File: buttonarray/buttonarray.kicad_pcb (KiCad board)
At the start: 2 copper layers, 129.5 x 106.7 mm, 103 parts, among them J1 CtrlPins, Q1 2N2219, Q10 2N2219, Q11 2N2219, Q12 2N2219, Q13 2N2219, Q14 2N2219, Q15 2N2219, Q16 2N2219, Q2 2N2219, Q3 2N2219, Q4 2N2219, Q5 2N2219, Q6 2N2219, Q7 2N2219, Q8 2N2219, Q9 2N2219, SW1 SW_Push_LED, SW10 SW_Push_LED, SW11 SW_Push_LED, SW12 SW_Push_LED, SW13 SW_Push_LED, SW14 SW_Push_LED, SW15 SW_Push_LED, SW16 SW_Push_LED, SW17 Addr_DIP_SW, SW2 SW_Push_LED, SW3 SW_Push_LED, SW4 SW_Push_LED, SW5 SW_Push_LED, SW6 SW_Push_LED, SW7 SW_Push_LED, SW8 SW_Push_LED, SW9 SW_Push_LED, U1 LM2575-3.3BT

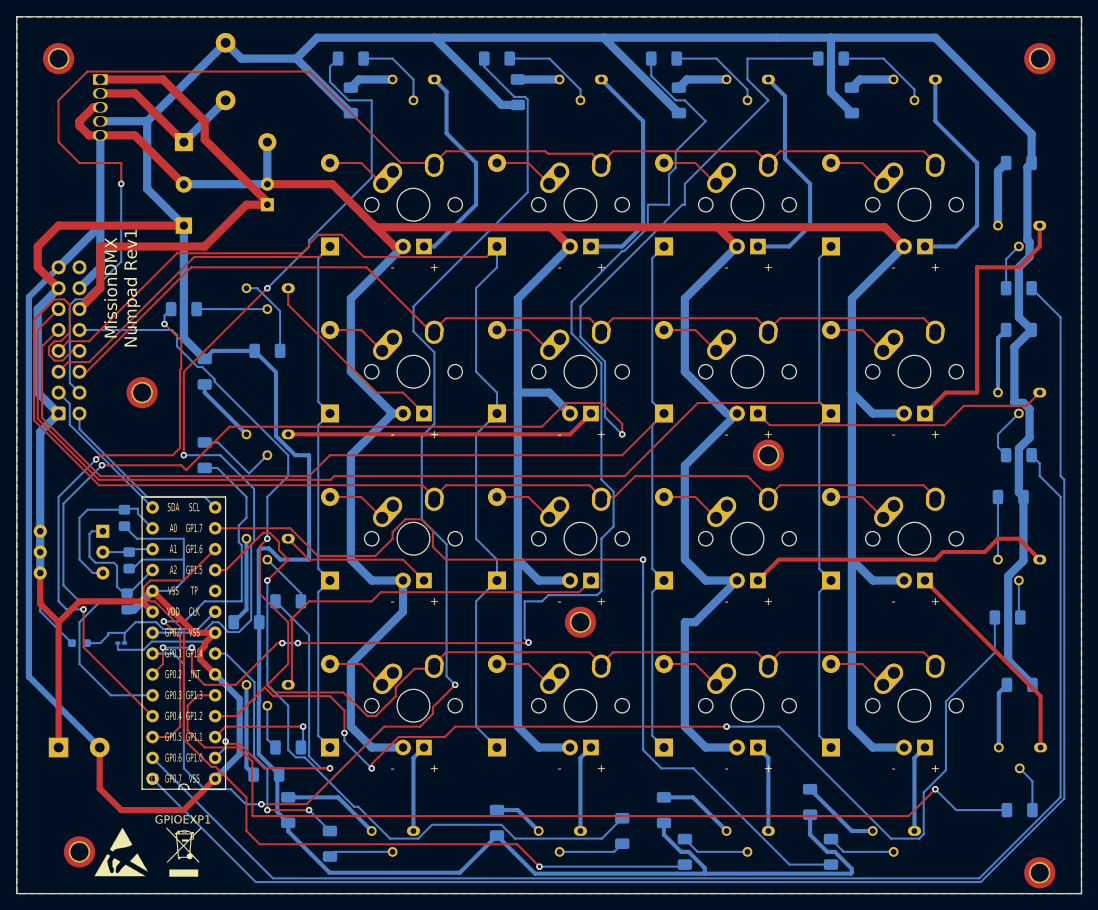
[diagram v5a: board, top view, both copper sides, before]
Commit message: chg: button array rev 1
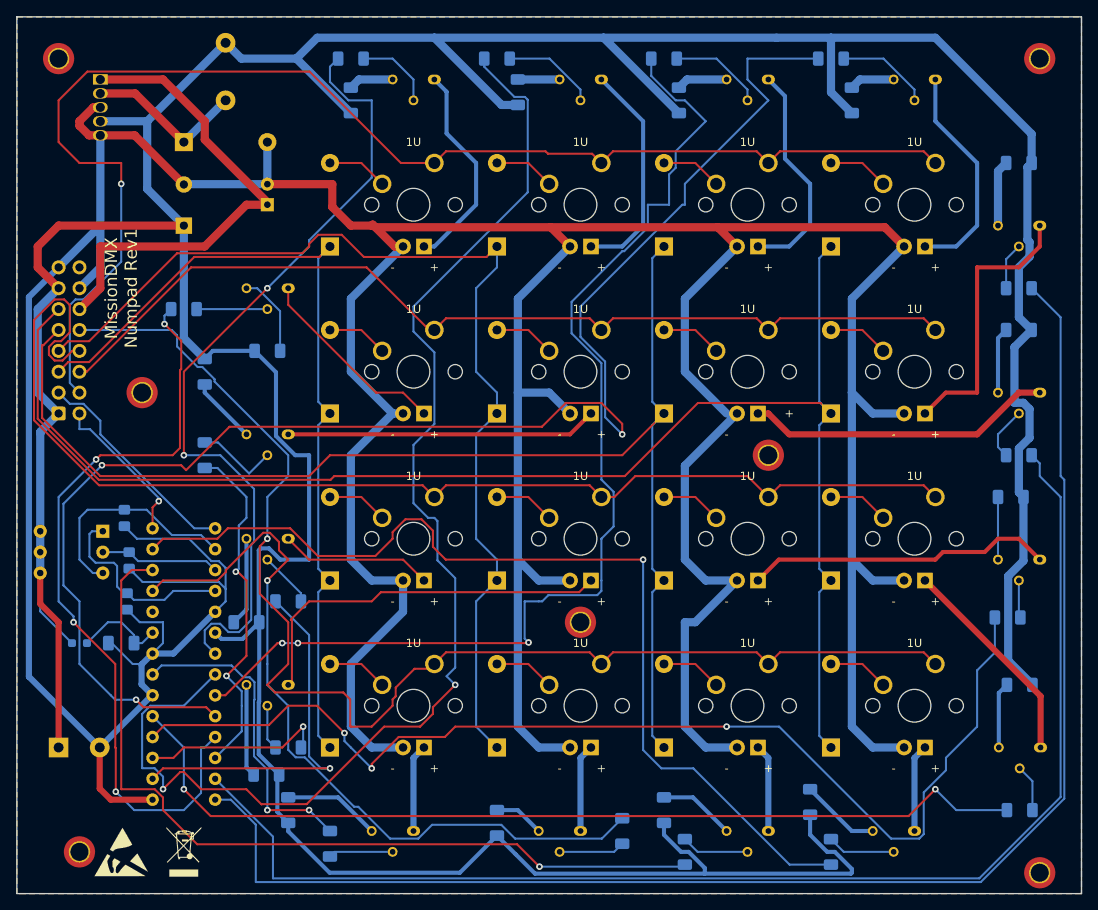
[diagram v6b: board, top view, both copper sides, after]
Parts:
- C1: footprint Capacitor_SMD:C_0201_0603Metric_Pad0.64x0.40mm_HandSolder -> Capacitor_SMD:C_1206_3216Metric_Pad1.33x1.80mm_HandSolder
- GPIOEXP1: moved to B.Cu
- SW1, SW10, SW11, SW12, SW13, SW14, SW15, SW16, SW2, SW3, SW4, SW5, SW6, SW7, SW8, SW9: footprint Mission_DMX_Footprint_Library:MX-1.0u-LED -> Mission_DMX_Footprint_Library:MXOnly-1U
- moved GPIOEXP1 8.03 mm to (69.8, 120.7), turned to 0 degrees
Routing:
- net LED5D: track 68.0 -> 94.1 mm, vias 3 -> 4
- net LED3D: track 148.4 -> 135.2 mm, vias 5 -> 3
- net LED2D: track 146.6 -> 156.9 mm
- net GND: track 642.9 -> 633.5 mm
- net LED14D: track 85.5 -> 94.3 mm
- net LED16D: track 110.8 -> 119.4 mm
- net LED10D: track 13.9 -> 22.6 mm
- net Net-(C1-Pad1): track 19.8 -> 11.2 mm
- net Net-(GPIOEXP1-Pad16): track 19.3 -> 27.5 mm
- net LED_I2C_SDA: track 18.7 -> 26.9 mm
- net Net-(GPIOEXP1-Pad17): track 6.72 -> 14.6 mm
- net LED13D: track 31.2 -> 38.6 mm
- net +3V3: track 554.9 -> 548.2 mm
- net Net-(GPIOEXP1-Pad18): track 17.7 -> 23.9 mm
- net LED7D: track 163.7 -> 158.0 mm
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- added copper zone on B.Cu, net +3V3
- added copper zone on F.Cu, net GND
- removed copper zone on F.Cu, net +3V3
- removed copper zone on B.Cu, net GND
